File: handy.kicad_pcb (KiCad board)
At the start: 2 copper layers, 69.1 x 9.1 mm, 20 parts, among them J1 JST-SH 1x4, J2 JST-SH 1x4, U1 TCA9548ARGER, U2 AS5600L-ASOM, U3 AS5600L-ASOM

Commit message: first draft
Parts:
- removed R5, R6: 4.7k, Resistor_SMD:R_0201_0603Metric
- removed REF**: MountingHole_2.2mm_M2_DIN965_Pad, MountingHole:MountingHole_2.2mm_M2_DIN965_Pad
- added H1: MountingHole, MountingHole:MountingHole_2.2mm_M2_ISO14580_Pad, F.Cu at (149.5, 100.0)
- added M1: Motor 1, Connector_PinHeader_2.00mm:PinHeader_1x02_P2.00mm_Vertical, F.Cu at (145.5, 101.5)
- added M2: Motor 2, Connector_PinHeader_2.00mm:PinHeader_1x02_P2.00mm_Vertical, F.Cu at (145.5, 98.5)
- added U4: DRV8830DGQR, DRV8830:DGQ10_2P18X1P72, F.Cu at (138.5, 100.0)
- added U5: ICM-42670-P, ICM42670:LGA14_2.5X3X0.76_IVS, F.Cu at (154.5, 100.0)
- C1, C2: footprint Capacitor_SMD:C_0603_1608Metric -> Capacitor_SMD:C_0201_0603Metric
- JP1, JP2, JP3: footprint Resistor_SMD:R_0201_0603Metric -> Resistor_SMD:R_0201_0603Metric_Pad0.64x0.40mm_HandSolder
- moved R9 39.5 mm to (125.5, 102.8), turned to 90 degrees
- moved R4 38.9 mm to (124.0, 98.3), turned to -90 degrees
- moved R7 37.9 mm to (132.5, 99.6), turned to 90 degrees
- moved R1 36.5 mm to (159.0, 97.8), turned to 90 degrees
- moved R2 34.6 mm to (161.0, 97.3), turned to 90 degrees
- moved R8 33.9 mm to (132.2, 97.8), turned to 180 degrees
- moved R3 33.3 mm to (124.0, 100.4), turned to 90 degrees
- moved JP1 19.7 mm to (133.9, 99.0)
- moved JP3 19.4 mm to (124.6, 102.8), turned to -90 degrees
- moved JP2 14.9 mm to (134.0, 97.8), turned to 180 degrees
- moved J2 5.50 mm to (165.2, 100.0)
- moved J1 4.52 mm to (171.2, 100.0)
- moved C1 2.52 mm to (124.3, 101.5), turned to 0 degrees
- moved C2 2.23 mm to (174.8, 98.4)
- moved U1 1.35 mm to (128.8, 100.5)
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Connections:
- U1 pad 1: unconnected-(U1-SD0-Pad1) -> /SDA0
- U1 pad 10: /SDA0 -> /SDA1
- U1 pad 11: /SCL0 -> /SCL1
- U1 pad 2: unconnected-(U1-SC0-Pad2) -> /SCL0
- U1 pad 7: /SDA1 -> unconnected-(U1-SD3-Pad7)
- U1 pad 8: /SCL1 -> unconnected-(U1-SC3-Pad8)
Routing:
- net +3.3V: track 12.5 -> 111.1 mm, vias 0 -> 3
- net /SDA0: track 2.02 -> 60.9 mm, vias 1 -> 2
- net /SCL0: track 2.10 -> 60.1 mm, vias 1 -> 4
- net /SDA: track 0.00 -> 44.6 mm
- net /SCL: track 0.00 -> 43.3 mm
- net GND: track 7.77 -> 26.9 mm, vias 4 -> 14
- net /M1: track 0.00 -> 14.3 mm
- net /M2: track 0.00 -> 11.5 mm
- net /SDA1: track 2.37 -> 11.7 mm, vias 1 -> 0
- net /SCL1: track 2.37 -> 10.7 mm, vias 1 -> 0
- net /ADDR_2: track 0.00 -> 6.04 mm
- net /ADDR_1: track 0.00 -> 4.39 mm
- net /ADDR_0: track 0.00 -> 3.47 mm

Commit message: fuck my chungus life
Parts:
- removed U5: ICM-42670-P, ICM42670:LGA14_2.5X3X0.76_IVS
- C1, C2: footprint Capacitor_SMD:C_0201_0603Metric -> Capacitor_SMD:C_0603_1608Metric
- JP1, JP2, JP3: footprint Resistor_SMD:R_0201_0603Metric_Pad0.64x0.40mm_HandSolder -> Jumper:SolderJumper-2_P1.3mm_Open_TrianglePad1.0x1.5mm
- R1, R2, R3, R4, R7, R8, R9: footprint Resistor_SMD:R_0201_0603Metric -> Resistor_SMD:R_0603_1608Metric
- moved R1 13.2 mm to (160.0, 84.7)
- moved C1 13.1 mm to (125.8, 88.5)
- moved C2 13.1 mm to (176.2, 85.4)
- moved H1 13.1 mm to (151.0, 87.0)
- moved J1 13.1 mm to (172.7, 87.0)
- moved J2 13.1 mm to (166.7, 87.0)
- moved JP1 13.1 mm to (135.4, 86.0)
- moved JP2 13.1 mm to (135.5, 84.8)
- moved M1 13.1 mm to (147.0, 88.5)
- moved M2 13.1 mm to (147.0, 85.5)
- moved R2 13.1 mm to (162.5, 84.3)
- moved R3 13.1 mm to (125.5, 87.4)
- moved R4 13.1 mm to (125.5, 85.3)
- moved R7 13.1 mm to (134.0, 86.6)
- moved R8 13.1 mm to (133.7, 84.8)
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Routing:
- net +3.3V: track 111.1 -> 0.00 mm, vias 3 -> 0
- net /SDA0: track 60.9 -> 0.00 mm, vias 2 -> 0
- net /SCL0: track 60.1 -> 0.00 mm, vias 4 -> 0
- net /SDA: track 44.6 -> 0.00 mm
- net /SCL: track 43.3 -> 0.00 mm
- net GND: track 26.9 -> 0.00 mm, vias 14 -> 0
- net /M1: track 14.3 -> 0.00 mm
- net /SDA1: track 11.7 -> 0.00 mm
- net /M2: track 11.5 -> 0.00 mm
- net /SCL1: track 10.7 -> 0.00 mm
- net /ADDR_2: track 6.04 -> 0.00 mm
- net /ADDR_1: track 4.39 -> 0.00 mm
- net /ADDR_0: track 3.47 -> 0.00 mm

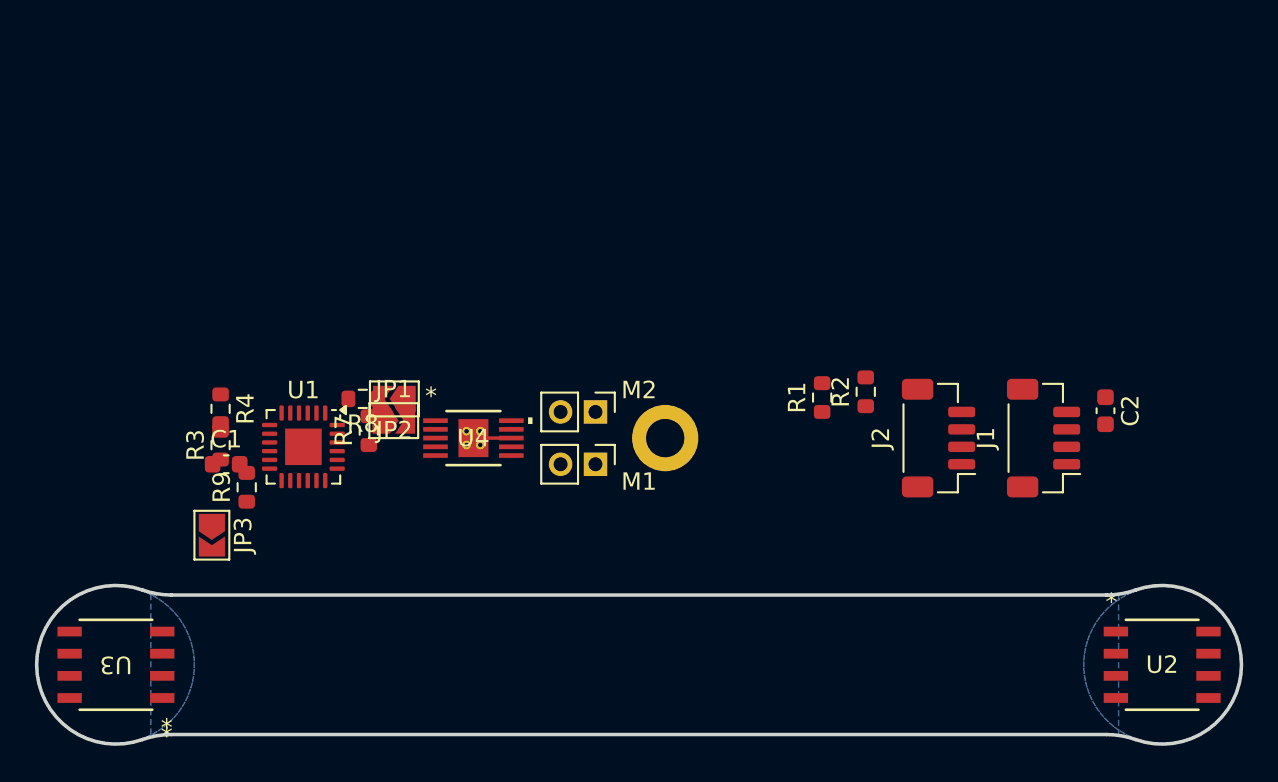
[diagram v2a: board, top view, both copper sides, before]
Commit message: routed without imu
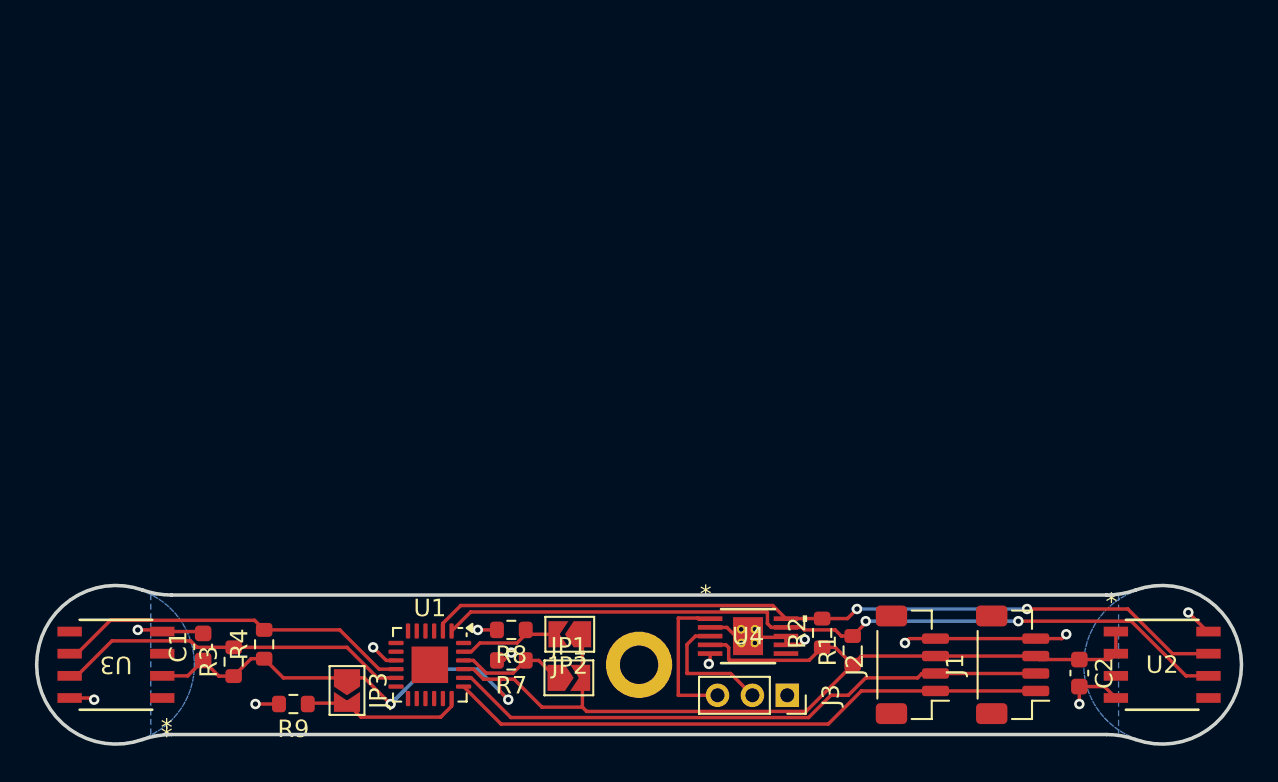
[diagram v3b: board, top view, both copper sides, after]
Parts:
- removed M1: Motor 1, Connector_PinHeader_2.00mm:PinHeader_1x02_P2.00mm_Vertical
- removed M2: Motor 2, Connector_PinHeader_2.00mm:PinHeader_1x02_P2.00mm_Vertical
- added J3: Conn_01x03_Pin, Connector_PinSocket_2.00mm:PinSocket_1x03_P2.00mm_Vertical, F.Cu at (158.0, 101.8)
- moved U4 19.4 mm to (155.8, 98.4)
- moved JP1 17.8 mm to (145.5, 100.8)
- moved JP2 16.8 mm to (145.5, 98.2)
- moved R8 15.8 mm to (142.2, 98.0)
- moved R7 15.5 mm to (142.2, 99.8), turned to 180 degrees
- moved C2 15.1 mm to (174.8, 100.5)
- moved R1 14.6 mm to (161.8, 99.2)
- moved U1 14.5 mm to (137.5, 100.0)
- moved R2 14.1 mm to (160.0, 98.2)
- moved R4 13.7 mm to (128.0, 98.8), turned to 90 degrees
- moved J1 13.1 mm to (170.9, 100.0)
- moved H1 13.1 mm to (149.5, 100.0)
- moved J2 13.1 mm to (165.2, 100.0)
- moved R9 12.7 mm to (129.7, 102.2), turned to 180 degrees
- moved R3 12.4 mm to (126.2, 99.8)
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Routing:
- net +3.3V: track 0.00 -> 81.0 mm, vias 0 -> 2
- net /SCL0: track 0.00 -> 46.9 mm, vias 0 -> 2
- net /SDA0: track 0.00 -> 46.5 mm, vias 0 -> 2
- net /SDA: track 0.00 -> 34.8 mm
- net /SCL: track 0.00 -> 34.5 mm
- net GND: track 0.00 -> 30.3 mm, vias 0 -> 12
- net /SDA1: track 0.00 -> 20.7 mm
- net /SCL1: track 0.00 -> 20.4 mm
- net /ADDR_2: track 0.00 -> 9.30 mm
- net /M2: track 0.00 -> 8.52 mm
- net /M1: track 0.00 -> 7.45 mm
- net /ADDR_0: track 0.00 -> 6.33 mm
- net /ADDR_1: track 0.00 -> 5.78 mm

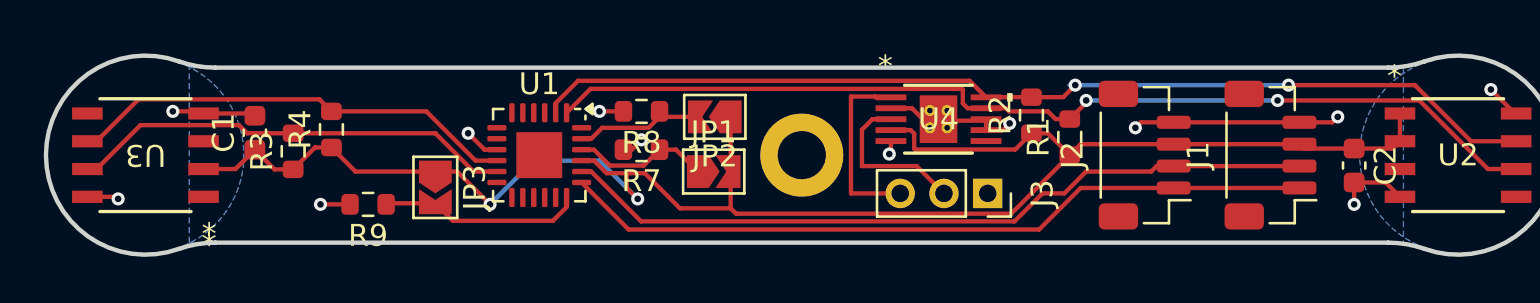
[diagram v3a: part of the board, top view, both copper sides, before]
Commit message: added missing pullup and capacitor
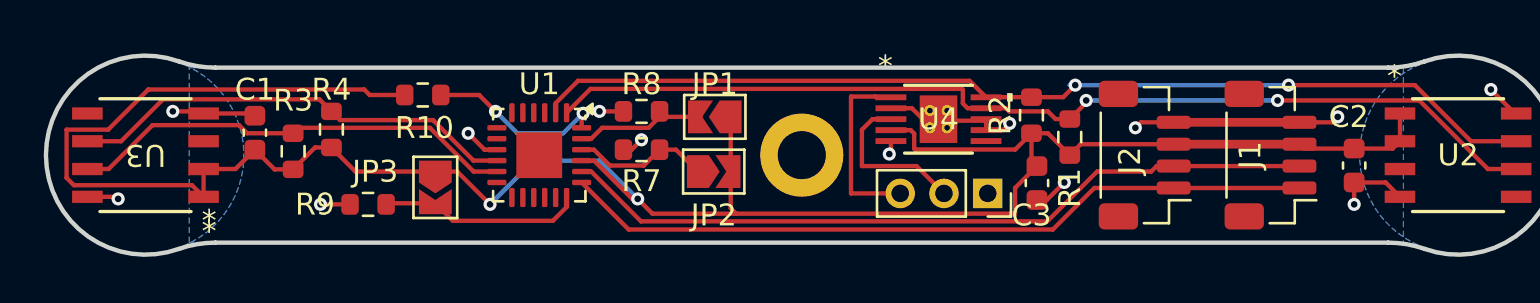
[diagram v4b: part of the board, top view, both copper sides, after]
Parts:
- added C3: 100uF, Capacitor_SMD:C_0603_1608Metric, F.Cu at (160.2, 101.3)
- added R10: 100k, Resistor_SMD:R_0603_1608Metric, F.Cu at (132.2, 97.2)
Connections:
- U1 pad 24: unconnected-(U1-~{RESET}-Pad24) -> Net-(U1-~{RESET})
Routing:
- net +3.3V: track 81.0 -> 107.0 mm
- net Net-(U1-~{RESET}): track 0.00 -> 8.30 mm, vias 0 -> 2
- net GND: track 30.3 -> 31.9 mm, vias 12 -> 13
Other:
- board text added: "David Cai 2025"
